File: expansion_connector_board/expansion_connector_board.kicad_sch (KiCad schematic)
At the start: 6 parts, among them J1 Conn_01x04, J12 Conn_02x17_Top_Bottom, J13 Conn_01x04, J3 Conn_02x17_Top_Bottom

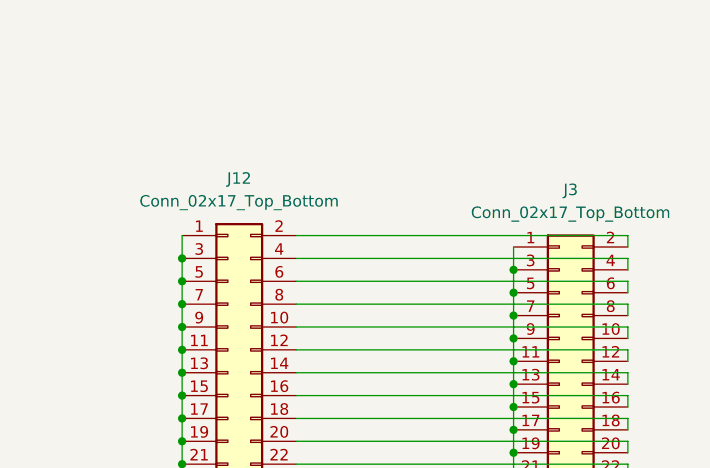
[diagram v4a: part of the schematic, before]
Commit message: update floppy header names to match underlying boards
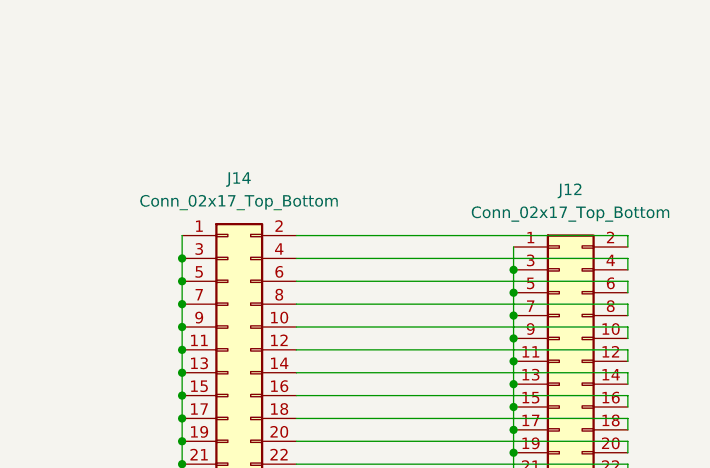
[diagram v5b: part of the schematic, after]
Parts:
- renumbered J3 to J12, J12 to J14
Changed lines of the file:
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@@
   (symbol (lib_id "Connector_Generic:Conn_02x17_Odd_Even") (at 170.18 66.04 0) (unit 1)
     (in_bom yes) (on_board yes) (fields_autoplaced)
-    (property "Reference" "J3" (id 0) (at 171.45 39.37 0))
+    (property "Reference" "J12" (id 0) (at 171.45 39.37 0))
     (property "Value" "Conn_02x17_Top_Bottom" (id 1) (at 171.45 41.91 0))
     (property "Footprint" "Connector_PinHeader_2.54mm:PinHeader_2x17_P2.54mm_Vertical" (id 2) (at 170.18 66.04 0)
@@
   (symbol (lib_id "Connector_Generic:Conn_02x17_Odd_Even") (at 133.35 64.77 0) (unit 1)
     (in_bom yes) (on_board yes) (fields_autoplaced)
-    (property "Reference" "J12" (id 0) (at 134.62 38.1 0))
+    (property "Reference" "J14" (id 0) (at 134.62 38.1 0))
     (property "Value" "Conn_02x17_Top_Bottom" (id 1) (at 134.62 40.64 0))
     (property "Footprint" "Connector_PinHeader_2.54mm:PinHeader_2x17_P2.54mm_Vertical" (id 2) (at 133.35 64.77 0)
@@
     )
     (path "/4641dd2b-8a78-420d-8cf9-d253cde42a58"
-      (reference "J3") (unit 1) (value "Conn_02x17_Top_Bottom") (footprint "Connector_PinHeader_2.54mm:PinHeader_2x17_P2.54mm_Vertical")
-    )
-    (path "/5e2b1b60-5db0-4075-8d2c-1c593da01486"
       (reference "J12") (unit 1) (value "Conn_02x17_Top_Bottom") (footprint "Connector_PinHeader_2.54mm:PinHeader_2x17_P2.54mm_Vertical")
     )
@@
       (reference "J13") (unit 1) (value "Conn_01x04") (footprint "Connector_PinHeader_2.54mm:PinHeader_1x04_P2.54mm_Vertical")
     )
+    (path "/5e2b1b60-5db0-4075-8d2c-1c593da01486"
+      (reference "J14") (unit 1) (value "Conn_02x17_Top_Bottom") (footprint "Connector_PinHeader_2.54mm:PinHeader_2x17_P2.54mm_Vertical")
+    )
     (path "/db6f34f2-3650-4262-8a8c-0ff568fe194f"

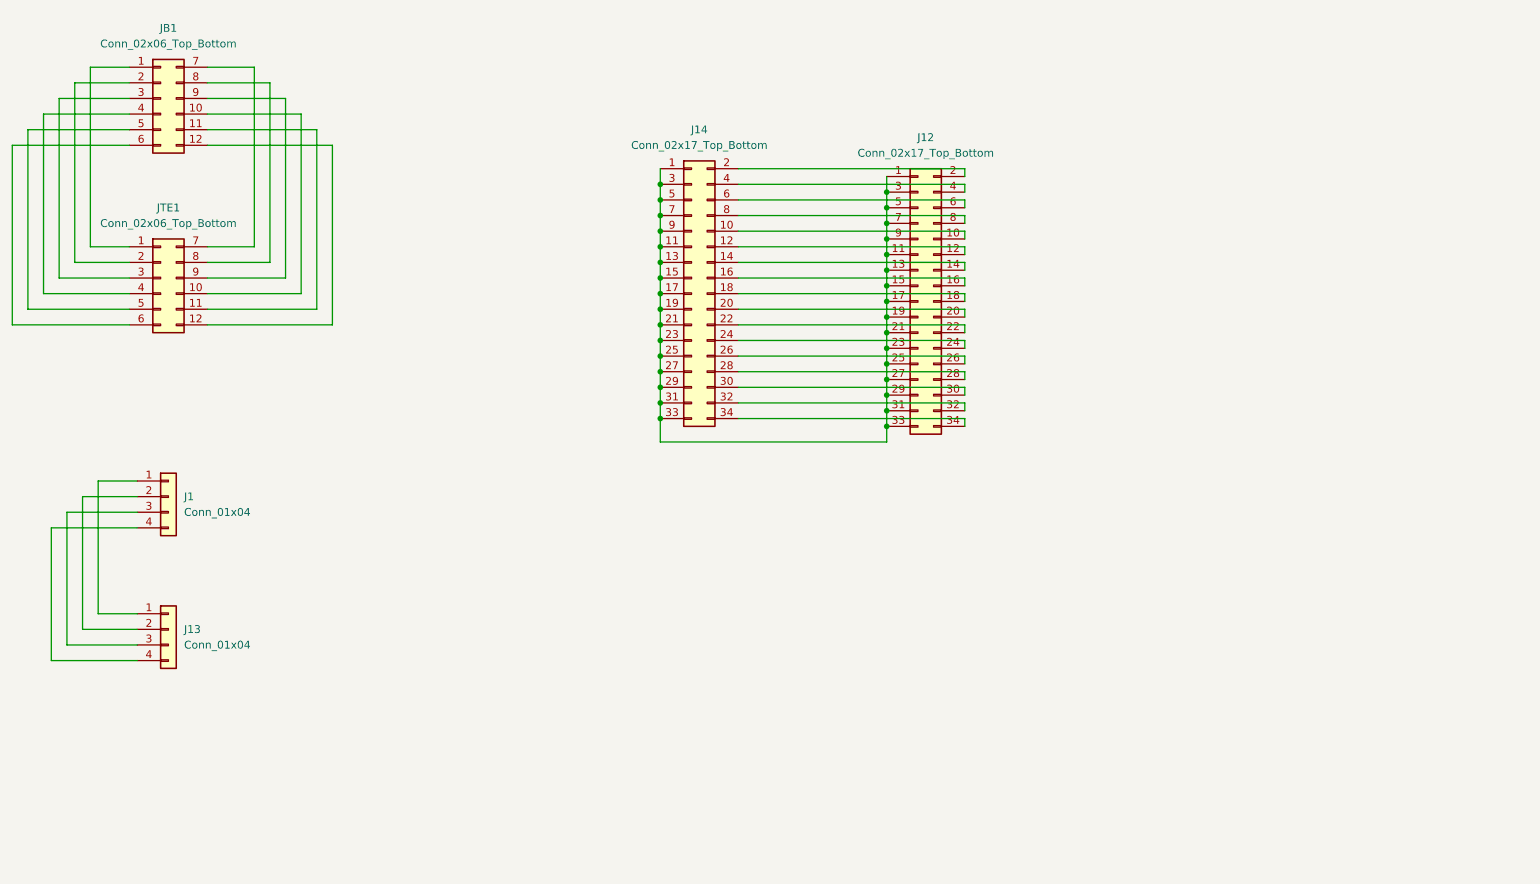
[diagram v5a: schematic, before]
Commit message: update to kicad 7. begin adding ESP32
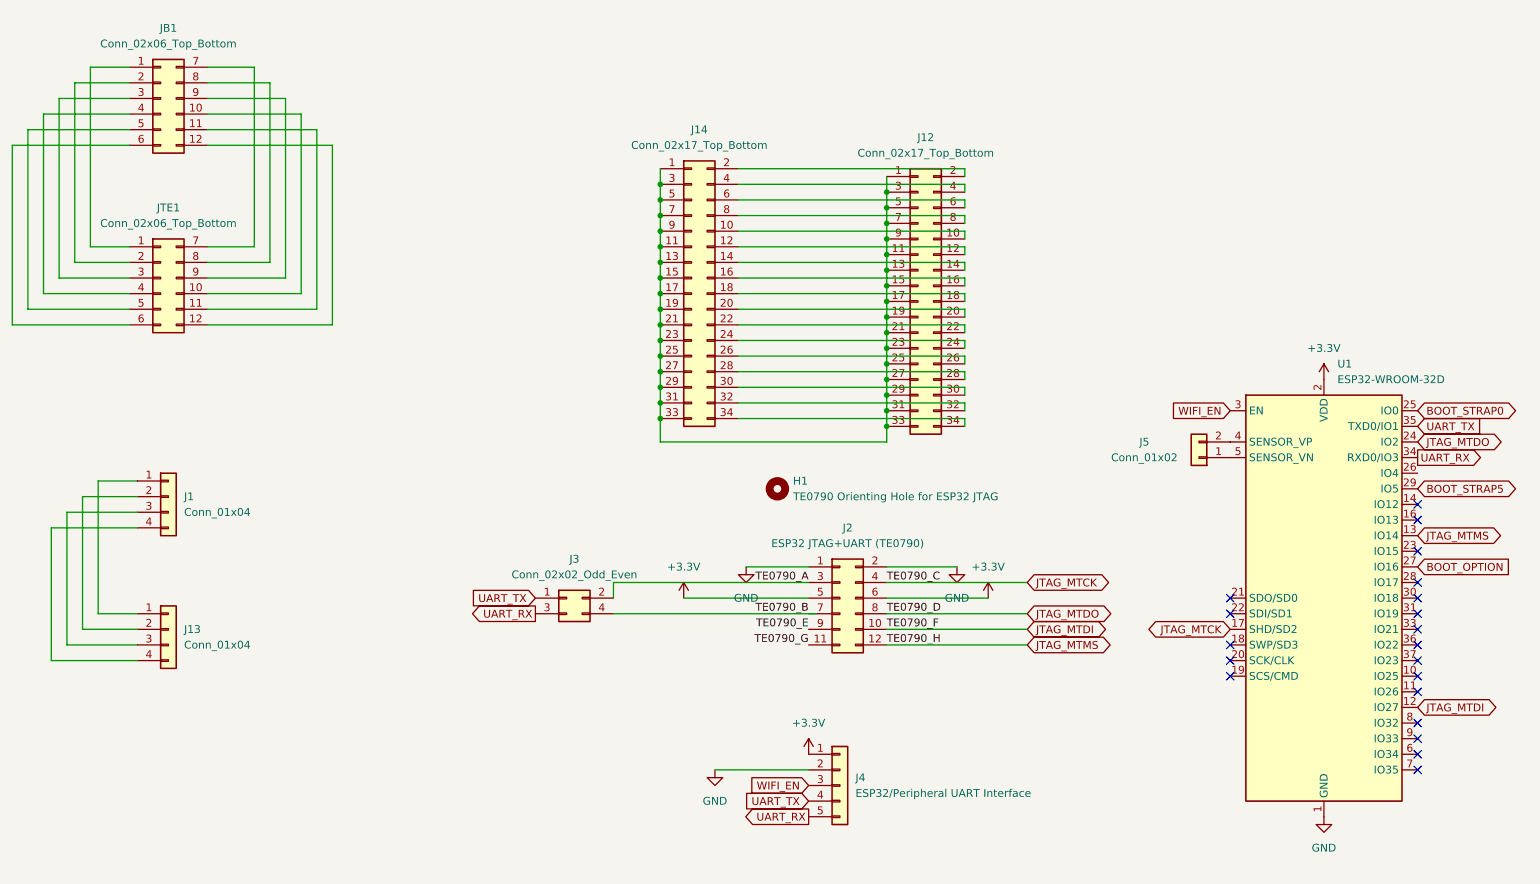
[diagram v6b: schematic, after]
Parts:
- added H1: TE0790 Orienting Hole for ESP32 JTAG, MountingHole:MountingHole_3.2mm_M3_Pad, symbol Mechanical:MountingHole
- added J2: ESP32 JTAG+UART (TE0790), Connector_PinHeader_2.54mm:PinHeader_2x06_P2.54mm_Vertical, symbol Connector_Generic:Conn_02x06_Odd_Even
- added J3: Conn_02x02_Odd_Even, symbol Connector_Generic:Conn_02x02_Odd_Even
- added J4: ESP32/Peripheral UART Interface, Connector_PinHeader_2.54mm:PinHeader_1x05_P2.54mm_Vertical, symbol Connector_Generic:Conn_01x05
- added J5: Conn_01x02, Connector_PinHeader_2.54mm:PinHeader_1x02_P2.54mm_Horizontal, symbol Connector_Generic:Conn_01x02
- added U1: ESP32-WROOM-32D, RF_Module:ESP32-WROOM-32D, symbol RF_Module:ESP32-WROOM-32D
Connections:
- new net: J5.1 (Pin_1), U1.5 (SENSOR_VN)
- new net: J5.2 (Pin_2), U1.4 (SENSOR_VP)
- new net +3.3V: J2.5 (Pin_5), J2.6 (Pin_6), J4.1 (Pin_1), U1.2 (VDD)
- new net BOOT_OPTION: U1.27 (IO16)
- new net BOOT_STRAP0: U1.25 (IO0)
- new net BOOT_STRAP5: U1.29 (IO5)
- new net GND: J2.1 (Pin_1), J2.2 (Pin_2), J4.2 (Pin_2), U1.1 (GND), U1.15 (GND), U1.38 (GND), U1.39 (GND)
- new net JTAG_MTCK: J2.4 (Pin_4), U1.17 (SHD/SD2)
- new net JTAG_MTDI: J2.10 (Pin_10), U1.12 (IO27)
- new net JTAG_MTDO: J2.8 (Pin_8), U1.24 (IO2)
- new net JTAG_MTMS: J2.12 (Pin_12), U1.13 (IO14)
- new net TE0790_A: J2.3 (Pin_3), J3.2 (Pin_2)
- new net TE0790_B: J2.7 (Pin_7), J3.4 (Pin_4)
- new net TE0790_E: J2.9 (Pin_9)
- new net TE0790_G: J2.11 (Pin_11)
- new net UART_RX: J3.3 (Pin_3), J4.5 (Pin_5), U1.34 (RXD0/IO3)
- new net UART_TX: J3.1 (Pin_1), J4.4 (Pin_4), U1.35 (TXD0/IO1)
- new net WIFI_EN: J4.3 (Pin_3), U1.3 (EN)
- no-connect marks 0 -> 20

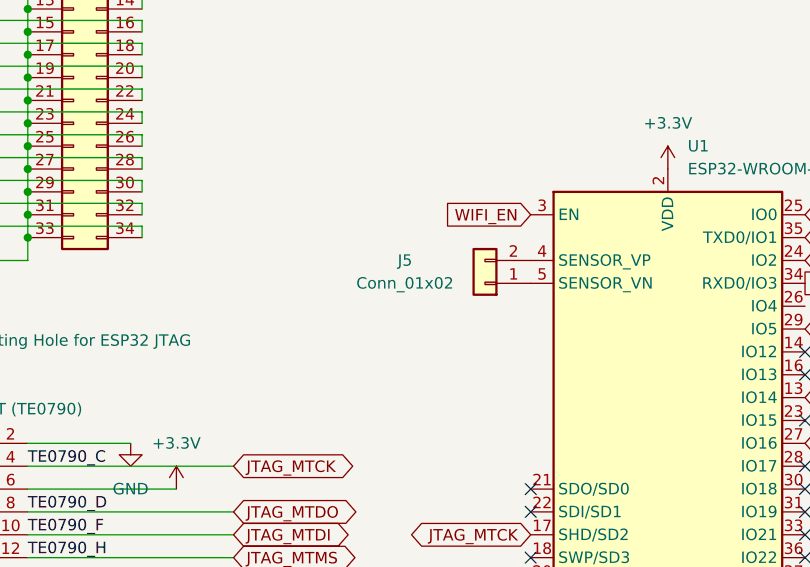
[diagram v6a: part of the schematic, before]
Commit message: finish adding ESP32 to bridge board
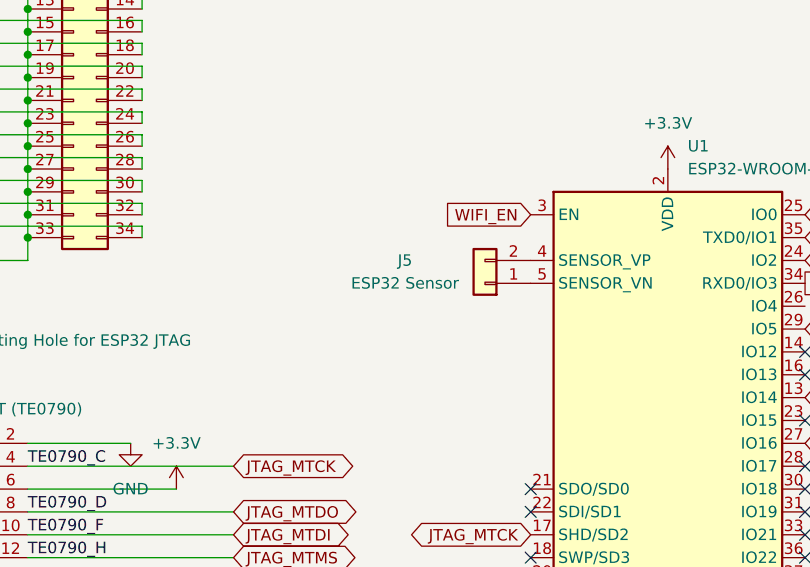
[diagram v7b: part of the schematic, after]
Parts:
- J5: value Conn_01x02 -> ESP32 Sensor
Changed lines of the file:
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@@
       (effects (font (size 1.27 1.27)))
     )
-    (property "Value" "Conn_01x02" (at 207.01 91.44 0)
+    (property "Value" "ESP32 Sensor" (at 207.01 91.44 0)
       (effects (font (size 1.27 1.27)))
     )

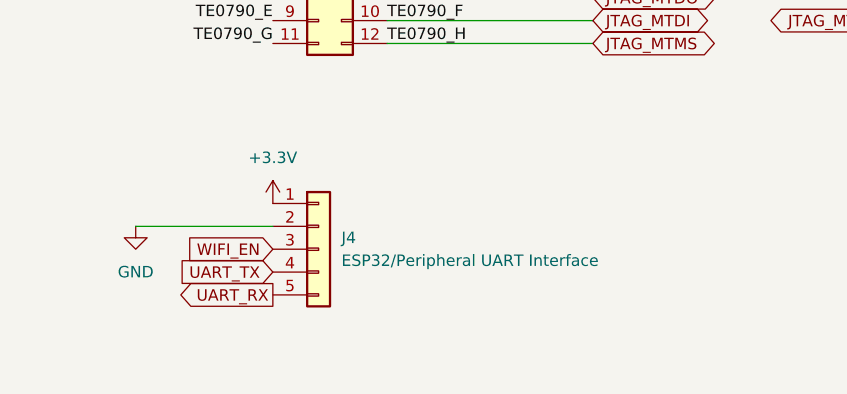
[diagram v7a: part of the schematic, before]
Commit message: add more pins to peripheral header. Reorder
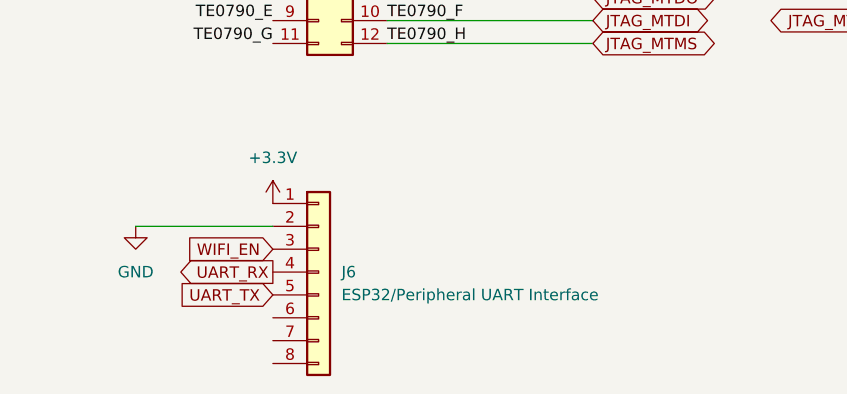
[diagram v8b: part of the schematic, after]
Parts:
- removed J4: ESP32/Peripheral UART Interface, Connector_PinHeader_2.54mm:PinHeader_1x05_P2.54mm_Vertical, symbol Connector_Generic:Conn_01x05
- added J6: ESP32/Peripheral UART Interface, Connector_PinHeader_2.54mm:PinHeader_1x08_P2.54mm_Vertical, symbol Connector_Generic:Conn_01x08
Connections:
- net +3.3V: now also J6.1 (Pin_1)
- net GND: now also J6.2 (Pin_2)
- net UART_RX: now also J6.4 (Pin_4)
- net UART_TX: now also J6.5 (Pin_5)
- net WIFI_EN: now also J6.3 (Pin_3)
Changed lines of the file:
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@@
     )
   )
-  (global_label "UART_RX" (shape output) (at 152.4 149.86 180) (fields_autoplaced)
+  (global_label "UART_RX" (shape output) (at 152.4 147.32 180) (fields_autoplaced)
     (effects (font (size 1.27 1.27)) (justify right))
-    (property "Intersheetrefs" "${INTERSHEET_REFS}" (at 141.311 149.86 0)
+    (property "Intersheetrefs" "${INTERSHEET_REFS}" (at 141.311 147.32 0)
       (effects (font (size 1.27 1.27)) (justify right) hide)
     )
@@
     )
   )
-  (global_label "UART_TX" (shape input) (at 152.4 147.32 180) (fields_autoplaced)
+  (global_label "UART_TX" (shape input) (at 152.4 149.86 180) (fields_autoplaced)
     (effects (font (size 1.27 1.27)) (justify right))
-    (property "Intersheetrefs" "${INTERSHEET_REFS}" (at 141.6134 147.32 0)
+    (property "Intersheetrefs" "${INTERSHEET_REFS}" (at 141.6134 149.86 0)
       (effects (font (size 1.27 1.27)) (justify right) hide)
     )
@@
         (path "/5cf04621-2344-4d80-a97f-45b514527429"
           (reference "#PWR04") (unit 1)
-        )
-      )
-    )
-  )
-  (symbol (lib_id "Connector_Generic:Conn_01x05") (at 157.48 144.78 0) (unit 1)
-    (in_bom yes) (on_board yes) (dnp no) (fields_autoplaced)
-    (property "Reference" "J4" (at 160.02 143.51 0)
-      (effects (font (size 1.27 1.27)) (justify left))
-    )
-    (property "Value" "ESP32/Peripheral UART Interface" (at 160.02 146.05 0)
-      (effects (font (size 1.27 1.27)) (justify left))
-    )
-    (property "Footprint" "Connector_PinHeader_2.54mm:PinHeader_1x05_P2.54mm_Vertical" (at 157.48 144.78 0)
-      (effects (font (size 1.27 1.27)) hide)
-    )
-    (property "Datasheet" "~" (at 157.48 144.78 0)
-      (effects (font (size 1.27 1.27)) hide)
-    )
-    (pin "1")
-    (pin "4")
-    (pin "2")
-    (pin "5")
-    (pin "3")
-    (instances
-      (project "expansion_connector_board"
-        (path "/5cf04621-2344-4d80-a97f-45b514527429"
-          (reference "J4") (unit 1)
         )
       )
@@
         )
       )
+    )
+  )
+  (symbol (lib_id "Connector_Generic:Conn_01x08") (at 157.48 147.32 0) (unit 1)
+    (in_bom yes) (on_board yes) (dnp no) (fields_autoplaced)
+    (property "Reference" "J6" (at 160.02 147.32 0)
+      (effects (font (size 1.27 1.27)) (justify left))
+    )
+    (property "Value" "ESP32/Peripheral UART Interface" (at 160.02 149.86 0)
+      (effects (font (size 1.27 1.27)) (justify left))
+    )
+    (property "Footprint" "Connector_PinHeader_2.54mm:PinHeader_1x08_P2.54mm_Vertical" (at 157.48 147.32 0)
+      (effects (font (size 1.27 1.27)) hide)
+    )
+    (property "Datasheet" "~" (at 157.48 147.32 0)
+      (effects (font (size 1.27 1.27)) hide)
+    )
+    (pin "8")
+    (pin "1")
+    (pin "7")
+    (pin "2")
+    (pin "4")
+    (pin "5")
+    (pin "3")
+    (pin "6")
+    (instances
+      (project "expansion_connector_board"
+        (path "/5cf04621-2344-4d80-a97f-45b514527429"
+          (reference "J6") (unit 1)
+        )
+      )
